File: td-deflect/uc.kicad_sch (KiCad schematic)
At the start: 26 parts, among them J16 Conn_02x10_Odd_Even, J4 Conn_ARM_JTAG_SWD_10, J6 Conn_01x06_Male, J7 Conn_02x10_Odd_Even, U12 LM1117-5.0, U2 STM32G473VETx, U23 TPS70933, U25 FM24C64B, U4 TPS70933, U8 INA181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

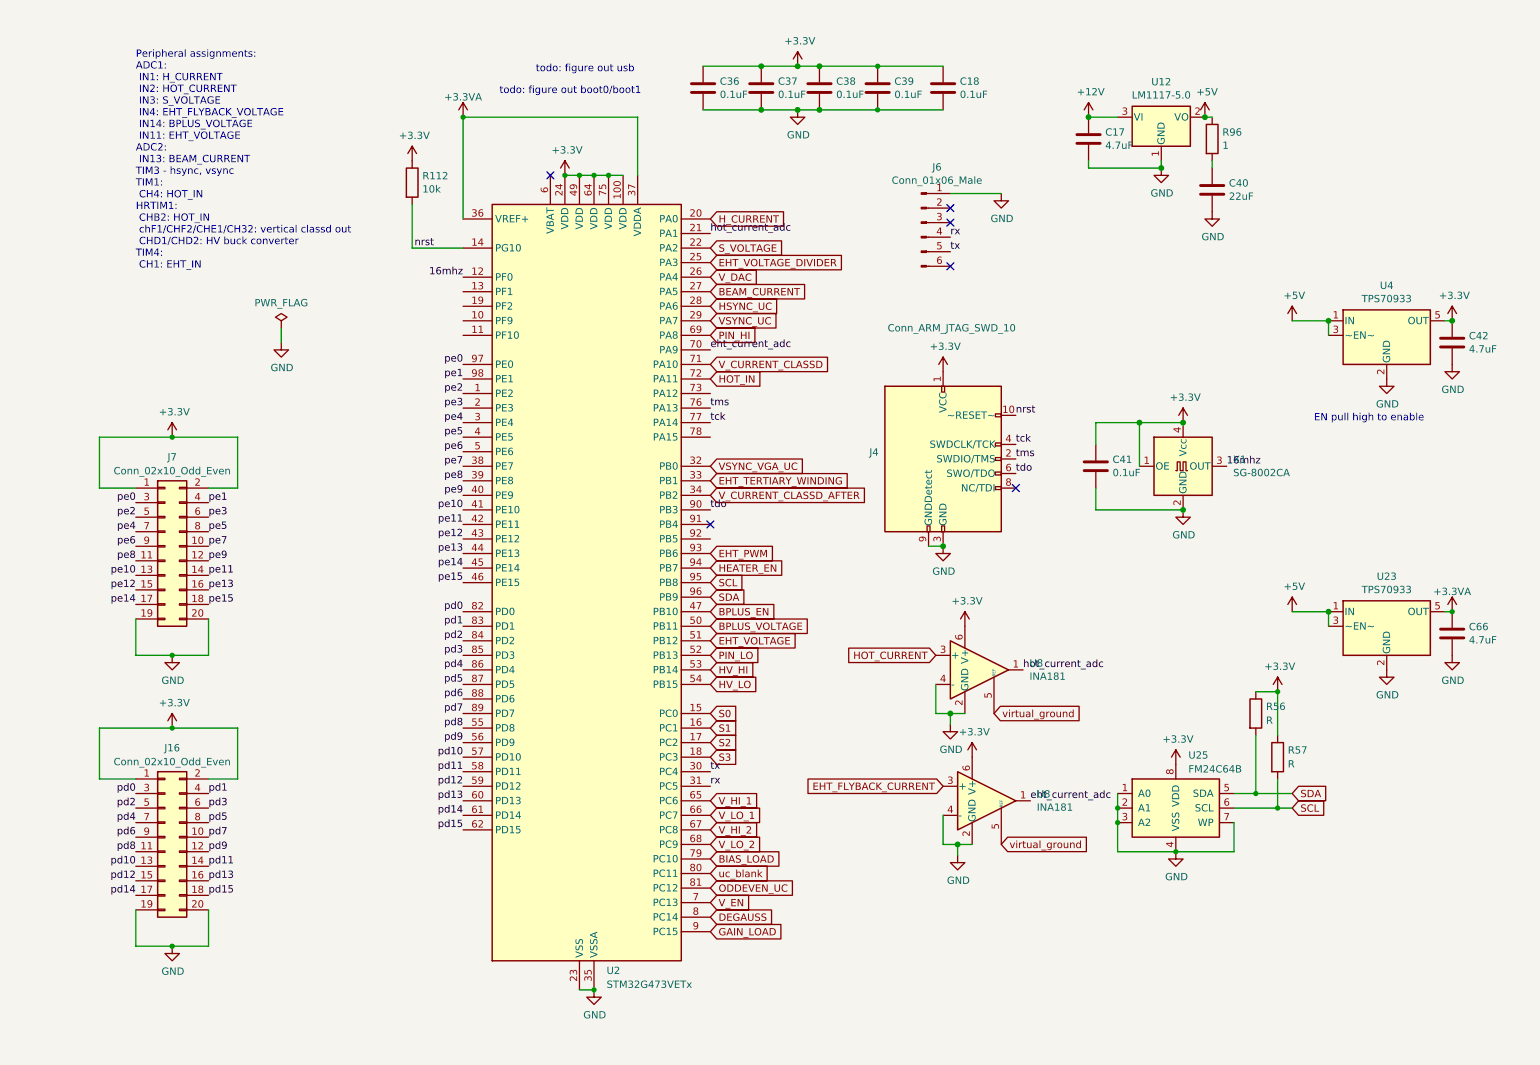
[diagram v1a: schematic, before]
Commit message: fix remaining erc errors
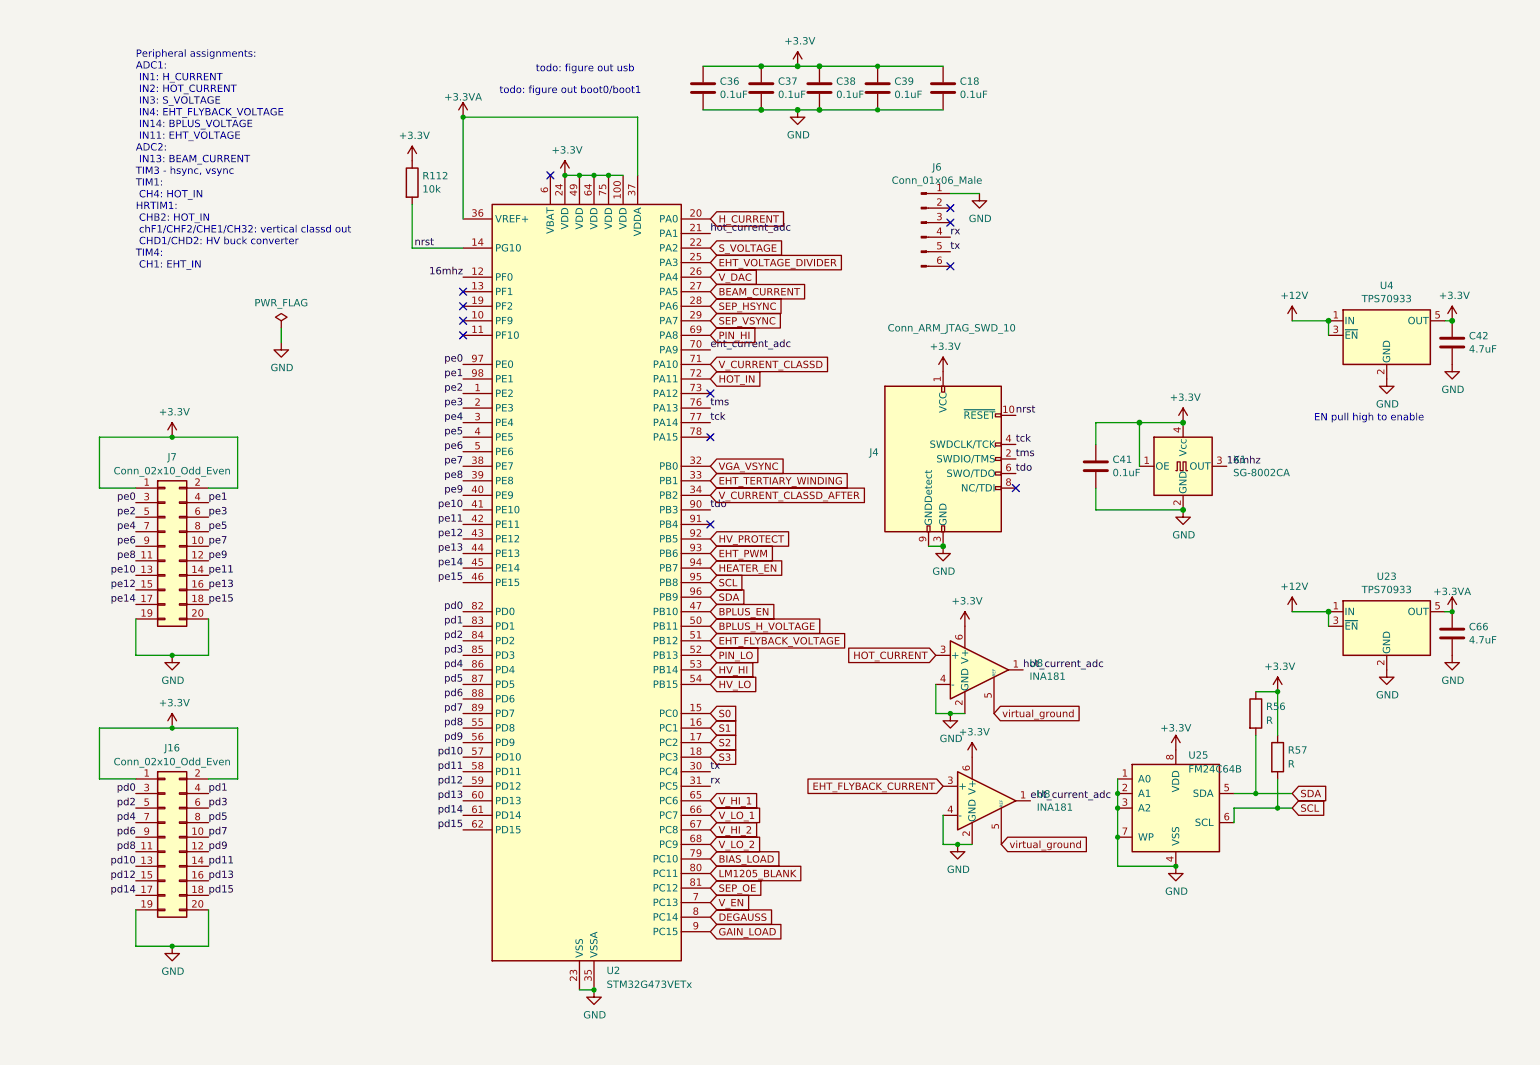
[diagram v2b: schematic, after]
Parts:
- removed C17: 4.7uF, Capacitor_SMD:C_0805_2012Metric_Pad1.18x1.45mm_HandSolder, symbol Device:C
- removed C40: 22uF, Capacitor_SMD:C_1206_3216Metric_Pad1.33x1.80mm_HandSolder, symbol Device:C
- removed R96: 1, Resistor_SMD:R_0805_2012Metric_Pad1.20x1.40mm_HandSolder, symbol Device:R
- removed U12: LM1117-5.0, Package_TO_SOT_SMD:TO-252-2, symbol Regulator_Linear:LM1117-3.3
- J6: symbol Connector:Conn_01x06_Male -> Connector:Conn_01x06_Pin
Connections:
- net +5V is gone; now on net +12V: U23.1 (IN), U23.3 (~{EN}), U4.1 (IN), U4.3 (~{EN})
- net HV_PROTECT: now reaches U2.92 (PB5)
- net +3V3 renamed +3.3V
- net BPLUS_VOLTAGE renamed BPLUS_H_VOLTAGE
- net EHT_VOLTAGE renamed EHT_FLYBACK_VOLTAGE
- net HSYNC_UC renamed SEP_HSYNC
- net ODDEVEN_UC renamed SEP_OE
- net VSYNC_UC renamed SEP_VSYNC
- net VSYNC_VGA_UC renamed VGA_VSYNC
- net uc_blank renamed LM1205_BLANK
- no-connect marks 6 -> 12

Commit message: usb
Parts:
- added J2: USB_C_Receptacle_USB2.0, symbol Connector:USB_C_Receptacle_USB2.0
- added R12: 10k, symbol Device:R
- added R13, R14: 5.1k, symbol Device:R
- added SW1: SW_SPST, symbol Switch:SW_SPST
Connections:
- net +3.3V: now also SW1.1 (A)
- net GND: now also J2.A1 (GND), J2.A12 (GND), J2.B1 (GND), J2.B12 (GND), J2.S1 (SHIELD), R12.2, R13.2, R14.2
- net HEATER_EN: no longer U2.94 (PB7)
- net HOT_IN: now also U2.71 (PA10); no longer U2.72 (PA11)
- net S0: now also U2.96 (PB9); no longer U2.15 (PC0)
- net SCL: now also U2.78 (PA15); no longer U2.95 (PB8)
- net SDA: now also U2.94 (PB7); no longer U2.96 (PB9)
- net V_CURRENT_CLASSD: now also U2.15 (PC0); no longer U2.71 (PA10)
- net USB_DP: now reaches U2.73 (PA12)
- net USB_DP: now also J2.A6 (D+), J2.B6 (D+)
- new net: J2.B5 (CC2), R14.1
- new net: J2.A4 (VBUS), J2.A9 (VBUS), J2.B4 (VBUS), J2.B9 (VBUS)
- new net: J2.A5 (CC1), R13.1
- new net BOOT0: R12.1, SW1.2 (B), U2.95 (PB8)
- new net USB_DM: J2.A7 (D-), J2.B7 (D-), U2.72 (PA11)
- no-connect marks 12 -> 13
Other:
- note added: "Peripheral assignments: ADC1: IN1: H_CURRENT IN2: HOT_CURRENT IN3: S_VOLTAGE IN4: EHT_FLYBACK_VOLTAGE IN6: V_CURRENT_CLASSD IN14: BPLUS_VOLTAGE IN11: EHT_VOLTAGE ADC2: IN13: BEAM_CURRENT TIM3 - hsync, vsync TIM1: CH3: HOT_IN HRTIM1: CHB1: HOT_IN chF1/CHF2/CHE1/CH32: vertical classd out CHD1/CHD2: HV buck converter TIM4: CH1: EHT_IN"
- note removed: "Peripheral assignments: ADC1: IN1: H_CURRENT IN2: HOT_CURRENT IN3: S_VOLTAGE IN4: EHT_FLYBACK_VOLTAGE IN14: BPLUS_VOLTAGE IN11: EHT_VOLTAGE ADC2: IN13: BEAM_CURRENT TIM3 - hsync, vsync TIM1: CH4: HOT_IN HRTIM1: CHB2: HOT_IN chF1/CHF2/CHE1/CH32: vertical classd out CHD1/CHD2: HV buck converter TIM4: CH1: EHT_IN"

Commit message: assign more footprints
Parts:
- J2: footprint (none) -> Connector_USB:USB_C_Receptacle_XKB_U262-16XN-4BVC11
- R12, R13, R14: footprint (none) -> Resistor_SMD:R_0805_2012Metric
- SW1: footprint (none) -> Button_Switch_SMD:SW_DPDT_CK_JS202011JCQN
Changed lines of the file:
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@@
       (effects (font (size 1.27 1.27)) (justify left))
     )
-    (property "Footprint" "" (at 239.522 31.75 90)
+    (property "Footprint" "Resistor_SMD:R_0805_2012Metric" (at 239.522 31.75 90)
       (effects (font (size 1.27 1.27)) hide)
     )
@@
       (effects (font (size 1.27 1.27)) (justify left))
     )
-    (property "Footprint" "" (at 269.24 27.94 0)
+    (property "Footprint" "Button_Switch_SMD:SW_DPDT_CK_JS202011JCQN" (at 269.24 27.94 0)
       (effects (font (size 1.27 1.27)) hide)
     )
@@
       (effects (font (size 1.27 1.27)))
     )
-    (property "Footprint" "" (at 215.9 35.56 0)
+    (property "Footprint" "Connector_USB:USB_C_Receptacle_XKB_U262-16XN-4BVC11" (at 215.9 35.56 0)
       (effects (font (size 1.27 1.27)) hide)
     )
@@
       (effects (font (size 1.27 1.27)) (justify left))
     )
-    (property "Footprint" "" (at 248.412 31.75 90)
+    (property "Footprint" "Resistor_SMD:R_0805_2012Metric" (at 248.412 31.75 90)
       (effects (font (size 1.27 1.27)) hide)
     )
@@
       (effects (font (size 1.27 1.27)) (justify left))
     )
-    (property "Footprint" "" (at 267.462 36.83 90)
-      (effects (font (size 1.27 1.27)) hide)
-    )
+    (property "Footprint" "Resistor_SMD:R_0805_2012Metric" (at 267.462 36.83 90)
+      (effects (font (size 1.27 1.27)) hide)
+    )

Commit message: more layout work
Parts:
- added C17, C19: 0.1uF, Capacitor_SMD:C_0805_2012Metric_Pad1.18x1.45mm_HandSolder, symbol Device:C
- U2: value STM32G473VETx -> STM32G474VETx; symbol MCU_ST_STM32G4:STM32G473VETx -> MCU_ST_STM32G4:STM32G474VETx
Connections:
- net +3.3V: no longer U8.6 (V+), U8.6 (V+)
- net +3.3VA: now also U8.6 (V+), U8.6 (V+), C17.1, C19.1
- net GND: now also C17.2, C19.2
- net HEATER_EN: now also U2.91 (PB4)
- no-connect marks 13 -> 12

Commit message: more layout
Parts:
- removed J7: Conn_02x10_Odd_Even, Connector_IDC:IDC-Header_2x10_P2.54mm_Vertical, symbol Connector_Generic:Conn_02x10_Odd_Even
- added C20: 4.7uF, Capacitor_SMD:C_0805_2012Metric_Pad1.18x1.45mm_HandSolder, symbol Device:C
- added F4: Polyfuse, Fuse:Fuse_0805_2012Metric, symbol Device:Polyfuse
- added J15: Conn_01x04_Pin, Connector_JST:JST_XH_B4B-XH-A_1x04_P2.50mm_Vertical, symbol Connector:Conn_01x04_Pin
- added J22, J23: Conn_02x05_Odd_Even, Connector_IDC:IDC-Header_2x05_P2.54mm_Vertical, symbol Connector_Generic:Conn_02x05_Odd_Even
- added U12: AP2204K-3.3, Package_TO_SOT_SMD:SOT-23-5, symbol Regulator_Linear:AP2204K-3.3
- added U13: TSOP43xx, OptoDevice:Vishay_MOLD-3Pin, symbol Interface_Optical:TSOP43xx
- U23: value TPS70933 -> AP2204K-5.0; symbol td-deflect-rescue:TPS76933-Regulator_Linear -> Regulator_Linear:AP2204K-5.0; Digikey 296-35483-1-ND -> (none)
- U4: value TPS70933 -> AP2204K-3.3; symbol td-deflect-rescue:TPS76933-Regulator_Linear -> Regulator_Linear:AP2204K-3.3
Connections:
- net pe0 is gone; now on net SEP_OE: U2.97 (PE0)
- net pe1 is gone; now on net BIAS_LOAD: U2.98 (PE1)
- net pe7 is gone; now on net LM1205_BLANK: U2.38 (PE7)
- net +12V: now also U12.1 (VIN), U12.3 (EN)
- net +3.3V: now also F4.2, J23.10 (Pin_10), U13.3 (Vs)
- net +3.3VA: now also C20.1, U12.5 (VOUT); no longer C66.1, U23.5 (OUT)
- net BIAS_LOAD: no longer U2.79 (PC10)
- net GND: now also C20.2, J15.4 (Pin_4), J22.9 (Pin_9), J23.9 (Pin_9), U12.2 (GND), U13.2 (GND)
- net LM1205_BLANK: no longer U2.80 (PC11)
- net SEP_OE: no longer U2.81 (PC12)
- net ir: now reaches U2.19 (PF2)
- net ir: now also U13.1 (OUT)
- net pe10 renamed lcd_a0
- net lcd_a0: now also J22.4 (Pin_4)
- net pe11 renamed lcd_cs
- net lcd_cs: now also J22.3 (Pin_3)
- net pe12 renamed lcd_sck
- net lcd_sck: now also J23.2 (Pin_2)
- net pe13 renamed lcd_si
- net lcd_si: now also J23.1 (Pin_1)
- net pe14 renamed lcd_so
- net lcd_so: now also J23.6 (Pin_6)
- net pe15: no longer names the net of U2.46 (PE15)
- net pe2 renamed beeper
- net beeper: now also J22.1 (Pin_1)
- net pe3 renamed sd_det
- net sd_det: now also J23.7 (Pin_7)
- net pe4 renamed sd_cs
- net sd_cs: now also J23.4 (Pin_4)
- net pe5 renamed btn_enc
- net btn_enc: now also J22.2 (Pin_2)
- net pe6 renamed lcd_rst
- net lcd_rst: now also J22.5 (Pin_5)
- net pe8 renamed btn_en1
- net btn_en1: now also J23.3 (Pin_3)
- net pe9 renamed btn_en2
- net btn_en2: now also J23.5 (Pin_5)
- new net +5V: C66.1, J22.10 (Pin_10), U23.5 (VOUT)
- new net power_serial2: F4.1, J15.1 (Pin_1)
- new net rx2: J15.3 (Pin_3), U2.80 (PC11)
- new net tx2: J15.2 (Pin_2), U2.79 (PC10)
- new net ws2811: J22.6 (Pin_6), U2.81 (PC12)
- no-connect marks 12 -> 15
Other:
- note removed: "EN pull high to enable"
- note removed: "todo: figure out boot0/boot1"
- note removed: "todo: figure out usb"
- moved on the sheet: J16

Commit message: more stuff
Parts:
- added C21: 0.1uF, Capacitor_SMD:C_0805_2012Metric_Pad1.18x1.45mm_HandSolder, symbol Device:C
- J16: value Conn_02x10_Odd_Even -> Conn_02x6_Odd_Even; footprint Connector_IDC:IDC-Header_2x10_P2.54mm_Vertical -> Connector_IDC:IDC-Header_2x06_P2.54mm_Vertical; symbol Connector_Generic:Conn_02x10_Odd_Even -> Connector_Generic:Conn_02x06_Odd_Even
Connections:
- net +3.3VA: now also C21.1
- net GND: now also J16.11 (Pin_11), J16.12 (Pin_12), C21.2; no longer J16.19 (Pin_19), J16.20 (Pin_20)
- net pd0: no longer J16.3 (Pin_3)
- net pd1: no longer J16.4 (Pin_4)
- net pd10: now also J16.5 (Pin_5); no longer J16.13 (Pin_13)
- net pd11: now also J16.6 (Pin_6); no longer J16.14 (Pin_14)
- net pd12: now also J16.7 (Pin_7); no longer J16.15 (Pin_15)
- net pd13: now also J16.8 (Pin_8); no longer J16.16 (Pin_16)
- net pd14: now also J16.9 (Pin_9); no longer J16.17 (Pin_17)
- net pd15: now also J16.10 (Pin_10); no longer J16.18 (Pin_18)
- net pd2: no longer J16.5 (Pin_5)
- net pd3: no longer J16.6 (Pin_6)
- net pd4: no longer J16.7 (Pin_7)
- net pd5: no longer J16.8 (Pin_8)
- net pd6: no longer J16.9 (Pin_9)
- net pd7: no longer J16.10 (Pin_10)
- net pd8: now also J16.3 (Pin_3); no longer J16.11 (Pin_11)
- net pd9: now also J16.4 (Pin_4); no longer J16.12 (Pin_12)
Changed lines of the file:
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@@
   (junction (at 227.33 33.02) (diameter 0) (color 0 0 0 0)
+  )
+  (junction (at 129.54 30.48) (diameter 0) (color 0 0 0 0)
   )
   (junction (at 121.92 182.88) (diameter 0) (color 0 0 0 0)
@@
     (stroke (width 0) (type solid))
   )
-  (wire (pts (xy 30.48 97.79) (xy 24.13 97.79))
-    (stroke (width 0) (type default))
-  )
   (wire (pts (xy 250.19 68.58) (xy 252.73 68.58))
     (stroke (width 0) (type default))
@@
     (stroke (width 0) (type solid))
   )
+  (wire (pts (xy 48.26 107.95) (xy 43.18 107.95))
+    (stroke (width 0) (type default))
+  )
   (wire (pts (xy 213.36 153.67) (xy 213.36 161.29))
     (stroke (width 0) (type default))
@@
     (stroke (width 0) (type default))
   )
-  (wire (pts (xy 24.13 97.79) (xy 24.13 88.9))
+  (wire (pts (xy 24.13 88.9) (xy 24.13 107.95))
     (stroke (width 0) (type default))
   )
@@
     (stroke (width 0) (type solid))
   )
-  (wire (pts (xy 48.26 97.79) (xy 48.26 88.9))
+  (wire (pts (xy 48.26 88.9) (xy 48.26 107.95))
     (stroke (width 0) (type default))
   )
@@
     (stroke (width 0) (type default))
   )
-  (wire (pts (xy 43.18 97.79) (xy 48.26 97.79))
+  (wire (pts (xy 129.54 30.48) (xy 133.35 30.48))
     (stroke (width 0) (type default))
   )
@@
   )
   (wire (pts (xy 184.15 43.815) (xy 189.23 43.815))
+    (stroke (width 0) (type default))
+  )
+  (wire (pts (xy 24.13 107.95) (xy 30.48 107.95))
     (stroke (width 0) (type default))
   )
@@
     (effects (font (size 1.27 1.27)) (justify right bottom))
   )
-  (label "pd2" (at 30.48 102.87 180) (fields_autoplaced)
-    (effects (font (size 1.27 1.27)) (justify right bottom))
-  )
   (label "ir" (at 99.06 63.5 180) (fields_autoplaced)
     (effects (font (size 1.27 1.27)) (justify right bottom))
@@
     (effects (font (size 1.27 1.27)) (justify left bottom))
   )
-  (label "pd3" (at 43.18 102.87 0) (fields_autoplaced)
-    (effects (font (size 1.27 1.27)) (justify left bottom))
-  )
   (label "nrst" (at 195.58 82.55 0) (fields_autoplaced)
     (effects (font (size 1.27 1.27)) (justify left bottom))
@@
     (effects (font (size 1.27 1.27)) (justify left bottom))
   )
-  (label "pd5" (at 43.18 105.41 0) (fields_autoplaced)
-    (effects (font (size 1.27 1.27)) (justify left bottom))
-  )
   (label "pd12" (at 99.06 147.32 180) (fields_autoplaced)
     (effects (font (size 1.27 1.27)) (justify right bottom))
@@
     (effects (font (size 1.27 1.27)) (justify left bottom))
   )
-  (label "pd4" (at 30.48 105.41 180) (fields_autoplaced)
-    (effects (font (size 1.27 1.27)) (justify right bottom))
-  )
   (label "lcd_si" (at 99.06 106.68 180) (fields_autoplaced)
     (effects (font (size 1.27 1.27)) (justify right bottom))
@@
     (effects (font (size 1.27 1.27)) (justify left bottom))
   )
-  (label "pd6" (at 30.48 107.95 180) (fields_autoplaced)
-    (effects (font (size 1.27 1.27)) (justify right bottom))
-  )
   (label "pd3" (at 99.06 124.46 180) (fields_autoplaced)
     (effects (font (size 1.27 1.27)) (justify right bottom))
@@
     (effects (font (size 1.27 1.27)) (justify right bottom))
   )
-  (label "pd0" (at 30.48 100.33 180) (fields_autoplaced)
-    (effects (font (size 1.27 1.27)) (justify right bottom))
-  )
   (label "16mhz" (at 99.06 58.42 180) (fields_autoplaced)
     (effects (font (size 1.27 1.27)) (justify right bottom))
@@
   )
   (label "rx2" (at 142.24 162.56 0) (fields_autoplaced)
-    (effects (font (size 1.27 1.27)) (justify left bottom))
-  )
-  (label "pd7" (at 43.18 107.95 0) (fields_autoplaced)
-    (effects (font (size 1.27 1.27)) (justify left bottom))
-  )
-  (label "pd1" (at 43.18 100.33 0) (fields_autoplaced)
     (effects (font (size 1.27 1.27)) (justify left bottom))
   )
@@
     )
   )
-  (symbol (lib_id "Connector_Generic:Conn_02x10_Odd_Even") (at 35.56 107.95 0) (unit 1)
+  (symbol (lib_id "Connector_Generic:Conn_02x06_Odd_Even") (at 35.56 113.03 0) (unit 1)
     (in_bom yes) (on_board yes) (dnp no) (fields_autoplaced)
-    (property "Reference" "J16" (at 36.83 92.3757 0)
-      (effects (font (size 1.27 1.27)))
-    )
-    (property "Value" "Conn_02x10_Odd_Even" (at 36.83 94.7999 0)
-      (effects (font (size 1.27 1.27)))
-    )
-    (property "Footprint" "Connector_IDC:IDC-Header_2x10_P2.54mm_Vertical" (at 35.56 107.95 0)
-      (effects (font (size 1.27 1.27)) hide)
-    )
-    (property "Datasheet" "~" (at 35.56 107.95 0)
+    (property "Reference" "J16" (at 36.83 102.5357 0)
+      (effects (font (size 1.27 1.27)))
+    )
+    (property "Value" "Conn_02x6_Odd_Even" (at 36.83 104.9599 0)
+      (effects (font (size 1.27 1.27)))
+    )
+    (property "Footprint" "Connector_IDC:IDC-Header_2x06_P2.54mm_Vertical" (at 35.56 113.03 0)
+      (effects (font (size 1.27 1.27)) hide)
+    )
+    (property "Datasheet" "~" (at 35.56 113.03 0)
       (effects (font (size 1.27 1.27)) hide)
     )
@@
     (pin "11")
     (pin "12")
-    (pin "13")
-    (pin "14")
-    (pin "15")
-    (pin "16")
-    (pin "17")
-    (pin "18")
-    (pin "19")
-    (pin "2")
-    (pin "20")
+    (pin "2")
     (pin "3")
     (pin "4")
@@
     )
   )
+  (symbol (lib_id "Device:C") (at 133.35 34.29 0) (unit 1)
+    (in_bom yes) (on_board yes) (dnp no)
+    (property "Reference" "C21" (at 136.271 33.1216 0)
+      (effects (font (size 1.27 1.27)) (justify left))
+    )
+    (property "Value" "0.1uF" (at 136.271 35.433 0)
+      (effects (font (size 1.27 1.27)) (justify left))
+    )
+    (property "Footprint" "Capacitor_SMD:C_0805_2012Metric_Pad1.18x1.45mm_HandSolder" (at 134.3152 38.1 0)
+      (effects (font (size 1.27 1.27)) hide)
+    )
+    (property "Datasheet" "~" (at 133.35 34.29 0)
+      (effects (font (size 1.27 1.27)) hide)
+    )
+    (property "Voltage" "10V" (at 133.35 34.29 0)
+      (effects (font (size 1.27 1.27)) hide)
+    )
+    (property "Digikey" "1276-1099-1-ND" (at 133.35 34.29 0)
+      (effects (font (size 1.27 1.27)) hide)
+    )
+    (pin "1")
+    (pin "2")
+    (instances
+      (project "td-deflect"
+        (path "/55a1a5e1-4d11-4c3e-b2b4-b9d50ddc5f9d/00000000-0000-0000-0000-00005c37bef7"
+          (reference "C21") (unit 1)
+        )
+      )
+    )
+  )
   (symbol (lib_id "Switch:SW_SPST") (at 269.24 27.94 270) (unit 1)
     (in_bom yes) (on_board yes) (dnp no) (fields_autoplaced)
@@
         )
       )
+    )
+  )
+  (symbol (lib_id "power:GND") (at 133.35 38.1 0) (unit 1)
+    (in_bom yes) (on_board yes) (dnp no)
+    (property "Reference" "#PWR019" (at 133.35 44.45 0)
+      (effects (font (size 1.27 1.27)) hide)
+    )
+    (property "Value" "GND" (at 133.477 42.4942 0)
+      (effects (font (size 1.27 1.27)))
+    )
+    (property "Footprint" "" (at 133.35 38.1 0)
+      (effects (font (size 1.27 1.27)) hide)
+    )
+    (property "Datasheet" "" (at 133.35 38.1 0)
+      (effects (font (size 1.27 1.27)) hide)
+    )
+    (pin "1")
+    (instances
+      (project "td-deflect"
+        (path "/55a1a5e1-4d11-4c3e-b2b4-b9d50ddc5f9d/00000000-0000-0000-0000-00005c37bef7"
+          (reference "#PWR019") (unit 1)
+        )
+      )
